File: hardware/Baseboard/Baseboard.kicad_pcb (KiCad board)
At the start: 2 copper layers, 160 x 160 mm, 77 parts, among them IC1 74HC00, IC10 W65C22, IC11 74HC148, IC12 74HC273, IC2 W65C02, IC3 74HC138, IC4 SYSTEM ROM, IC5 RAM, IC6 W65C22, IC7 W65C51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

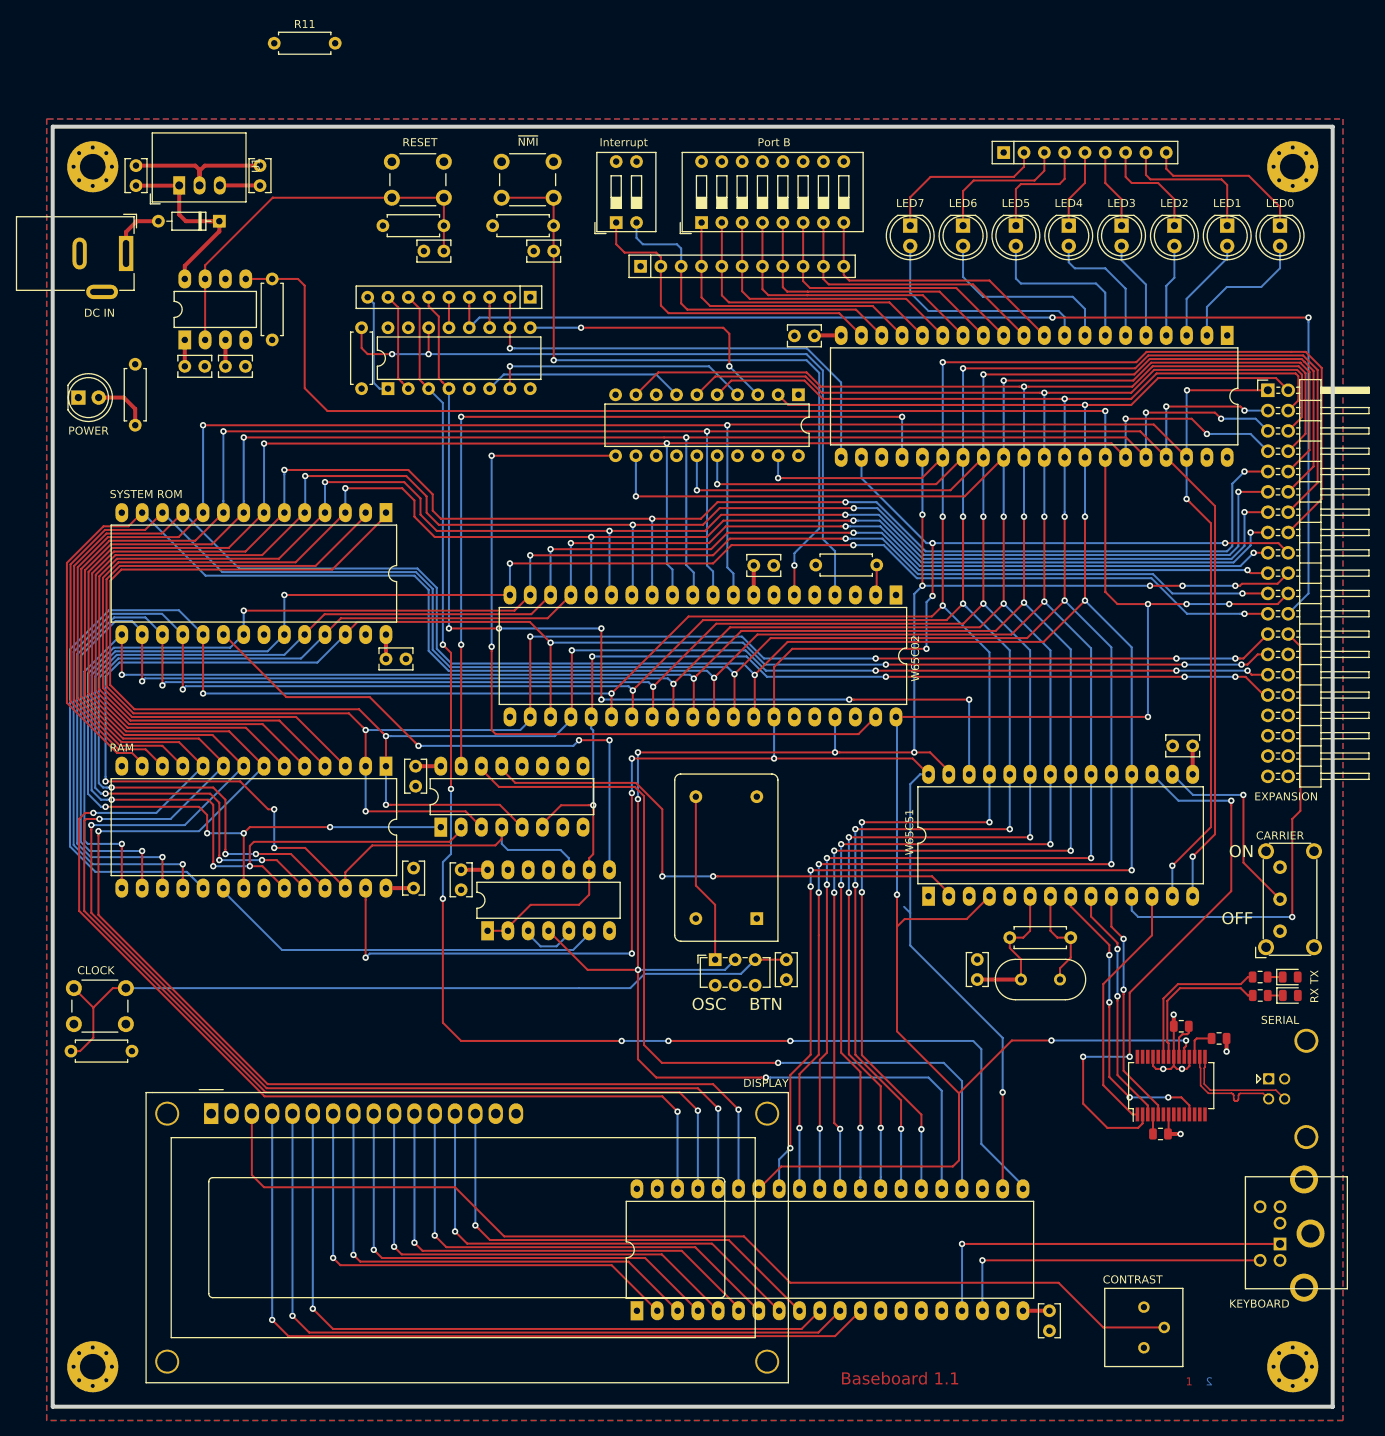
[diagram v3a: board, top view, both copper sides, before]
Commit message: Improve routing, add some datasheet recommendations
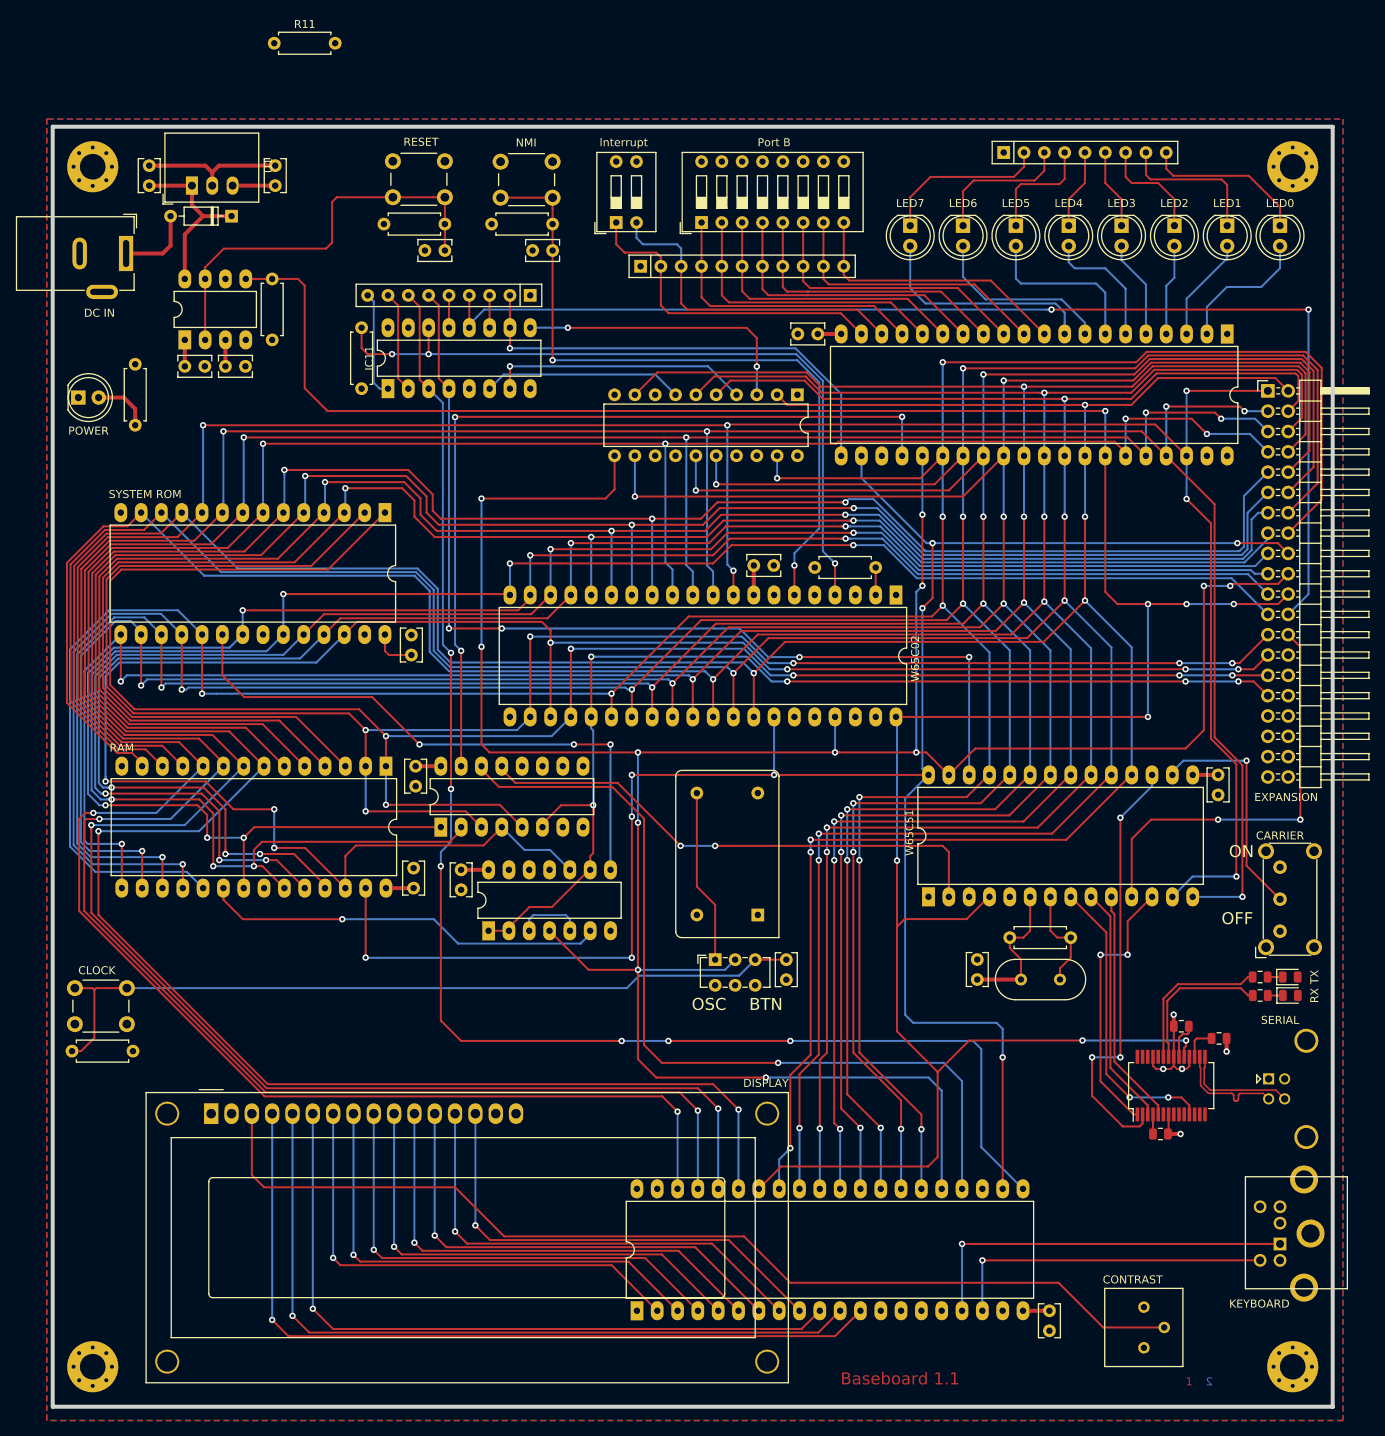
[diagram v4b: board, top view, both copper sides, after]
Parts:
- IC11: footprint Package_DIP:DIP-16_W7.62mm -> Package_DIP:DIP-16_W7.62mm_LongPads
- SW4: value ~NMI -> NMI
- moved C6 4.82 mm to (283.7, 132.3), turned to 270 degrees
- moved C4 3.21 mm to (182.9, 117.3), turned to 90 degrees
- moved C10 1.91 mm to (165.9, 58.7)
- moved C9 1.65 mm to (150.1, 58.7)
- moved D10 1.65 mm to (160.4, 62.5)
- moved U1 1.59 mm to (155.4, 58.7)
- moved C7 0.48 mm to (233.7, 77.2)
- moved XTAL1 0.47 mm to (226.2, 149.8)
- moved R3 0.34 mm to (233.3, 106.4)
- moved R5 0.24 mm to (179.5, 63.5)
- moved R9 0.24 mm to (192.9, 63.5)
- moved RN3 0.23 mm to (197.7, 72.4)
- moved IC6 0.18 mm to (284.9, 77.2)
- moved C17 0.16 mm to (200.5, 66.8)
- moved C11 0.15 mm to (187.1, 66.8)
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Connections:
- net /IO/~NMI renamed /IRQ/~NMI
- IC10 pad 13: Net-(IC10-Pad13) -> (no net)
- IC10 pad 14: Net-(IC10-Pad14) -> (no net)
- IC10 pad 15: Net-(IC10-Pad15) -> (no net)
- IC10 pad 16: Net-(IC10-Pad16) -> (no net)
- IC10 pad 19: Net-(IC10-Pad19) -> (no net)
- IC10 pad 39: Net-(IC10-Pad39) -> (no net)
- IC10 pad 40: Net-(IC10-Pad40) -> (no net)
- IC11 pad 15: Net-(IC11-Pad15) -> (no net)
- IC12 pad 11: /IRQ/IRQ_Sync -> /IO/Clock
- IC12 pad 13: Net-(IC12-Pad13) -> (no net)
- IC12 pad 14: Net-(IC12-Pad14) -> (no net)
- IC12 pad 17: Net-(IC12-Pad17) -> (no net)
- IC12 pad 18: Net-(IC12-Pad18) -> (no net)
- IC12 pad 8: Net-(IC12-Pad8) -> (no net)
- IC2 pad 1: Net-(IC2-Pad1) -> /IRQ/~IRQ_Read
- IC2 pad 3: Net-(IC2-Pad3) -> (no net)
- IC2 pad 35: Net-(IC2-Pad35) -> (no net)
- IC2 pad 36: Net-(IC2-Pad36) -> +5V
- IC2 pad 38: Net-(IC2-Pad38) -> +5V
- IC2 pad 39: /IRQ/IRQ_Sync -> (no net)
- IC2 pad 5: Net-(IC2-Pad5) -> (no net)
- IC2 pad 7: Net-(IC2-Pad7) -> (no net)
- IC3 pad 10: Net-(IC3-Pad10) -> (no net)
- IC3 pad 11: Net-(IC3-Pad11) -> (no net)
- IC3 pad 12: Net-(IC3-Pad12) -> (no net)
- IC3 pad 7: Net-(IC3-Pad7) -> (no net)
- IC3 pad 9: Net-(IC3-Pad9) -> (no net)
- IC6 pad 18: /IO/CB1 -> /IO/CB0
- IC6 pad 19: /IO/CB2 -> /IO/CB1
- IC6 pad 39: Net-(IC6-Pad39) -> (no net)
- IC6 pad 40: Net-(IC6-Pad40) -> (no net)
- IC7 pad 5: Net-(IC7-Pad5) -> (no net)
- IC8 pad 6: Net-(IC8-Pad6) -> (no net)
- IC9 pad 10: Net-(IC9-Pad10) -> (no net)
- IC9 pad 12: Net-(IC9-Pad12) -> (no net)
- IC9 pad 13: Net-(IC9-Pad13) -> (no net)
- IC9 pad 14: Net-(IC9-Pad14) -> (no net)
- IC9 pad 26: Net-(IC9-Pad26) -> (no net)
- IC9 pad 27: Net-(IC9-Pad27) -> (no net)
- IC9 pad 28: Net-(IC9-Pad28) -> (no net)
- IC9 pad 6: Net-(IC9-Pad6) -> (no net)
- IC9 pad 9: Net-(IC9-Pad9) -> (no net)
- RN1 pad 2: /IO/CB2 -> /IO/CB1
- RN1 pad 3: /IO/CB1 -> /IO/CB0
- RV1 pad 3: Net-(RV1-Pad3) -> (no net)
- SW2 pad 1: /IO/CB2 -> /IO/CB1
- SW2 pad 2: /IO/CB1 -> /IO/CB0
- X2 pad 1: Net-(X2-Pad1) -> (no net)
- X3 pad 28: Net-(X3-Pad28) -> (no net)
- X3 pad 30: Net-(X3-Pad30) -> (no net)
- X3 pad 32: Net-(X3-Pad32) -> (no net)
- X3 pad 33: Net-(X3-Pad33) -> (no net)
- X3 pad 34: Net-(X3-Pad34) -> (no net)
- X3 pad 35: Net-(X3-Pad35) -> (no net)
- X3 pad 36: Net-(X3-Pad36) -> (no net)
- X3 pad 37: Net-(X3-Pad37) -> (no net)
- X3 pad 38: Net-(X3-Pad38) -> (no net)
- X4 pad 2: Net-(X4-Pad2) -> (no net)
- X4 pad 6: Net-(X4-Pad6) -> (no net)
- XTAL1 pad 1: Net-(XTAL1-Pad1) -> (no net)
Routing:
- net /IRQ/IRQ_Sync: track 98.9 -> 0.00 mm, vias 2 -> 0
- net /IO/Clock: track 244.6 -> 333.8 mm, vias 11 -> 12
- net /IO/CB2: track 41.6 -> 0.00 mm
- net /IO/CB0: track 0.00 -> 41.6 mm
- net /Processor/~ModemReady: track 70.3 -> 54.5 mm
- net /IO/A1: track 414.8 -> 421.2 mm
- net /IO/A0: track 412.5 -> 418.2 mm, vias 7 -> 8
- net /IO/~TerminalReady: track 58.6 -> 53.0 mm, vias 1 -> 2
- net /IO/R~W: track 269.8 -> 264.3 mm, vias 10 -> 9
- net /IO/D0: track 393.3 -> 388.8 mm, vias 8 -> 7
- net /IO/~CarrierDetect: track 24.9 -> 29.3 mm
- net /IO/D2: track 399.5 -> 395.4 mm, vias 8 -> 7
- net /IO/D1: track 400.4 -> 396.3 mm, vias 8 -> 7
- net Net-(C11-Pad1): track 49.4 -> 52.3 mm
- net /IO/~Reset: track 344.5 -> 341.9 mm
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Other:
- net class Address removed

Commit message: Optimize routing
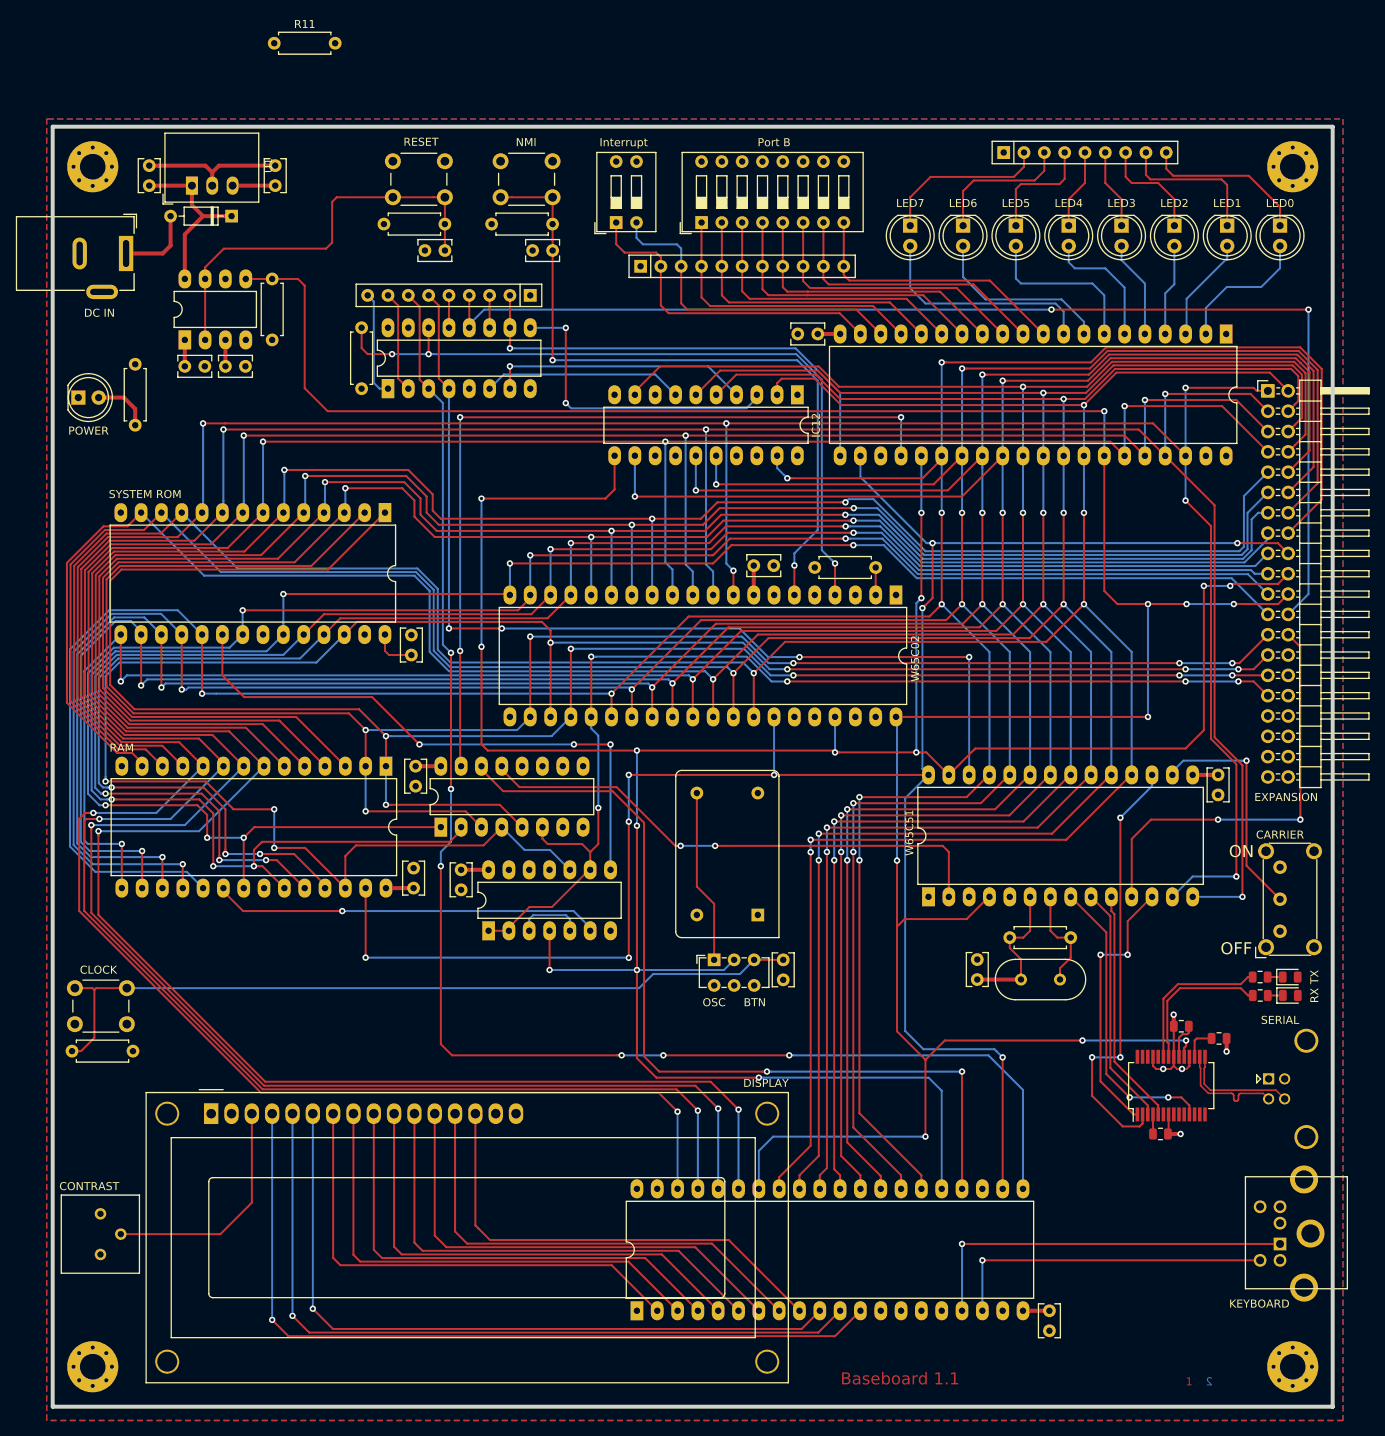
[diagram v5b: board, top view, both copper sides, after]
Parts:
- IC12: footprint Package_DIP:DIP-20_W7.62mm -> Package_DIP:DIP-20_W7.62mm_LongPads
- moved RV1 130.9 mm to (144.0, 192.3)
- moved C19 0.39 mm to (229.4, 155.4)
- moved SW7 0.13 mm to (220.7, 155.4)
- moved IC6 0.13 mm to (284.7, 77.2)
- moved SW4 0.05 mm to (194.0, 55.6)
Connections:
- IC10 pad 13: (no net) -> Net-(IC10-Pad13)
- IC10 pad 14: (no net) -> Net-(IC10-Pad14)
- IC10 pad 15: (no net) -> Net-(IC10-Pad15)
- IC10 pad 16: (no net) -> Net-(IC10-Pad16)
- IC10 pad 19: (no net) -> Net-(IC10-Pad19)
- IC10 pad 39: (no net) -> Net-(IC10-Pad39)
- IC10 pad 40: (no net) -> Net-(IC10-Pad40)
- IC11 pad 15: (no net) -> Net-(IC11-Pad15)
- IC12 pad 13: (no net) -> Net-(IC12-Pad13)
- IC12 pad 14: (no net) -> Net-(IC12-Pad14)
- IC12 pad 17: (no net) -> Net-(IC12-Pad17)
- IC12 pad 18: (no net) -> Net-(IC12-Pad18)
- IC12 pad 8: (no net) -> Net-(IC12-Pad8)
- IC2 pad 3: (no net) -> Net-(IC2-Pad3)
- IC2 pad 35: (no net) -> Net-(IC2-Pad35)
- IC2 pad 39: (no net) -> Net-(IC2-Pad39)
- IC2 pad 5: (no net) -> Net-(IC2-Pad5)
- IC2 pad 7: (no net) -> Net-(IC2-Pad7)
- IC3 pad 10: (no net) -> Net-(IC3-Pad10)
- IC3 pad 11: (no net) -> Net-(IC3-Pad11)
- IC3 pad 12: (no net) -> Net-(IC3-Pad12)
- IC3 pad 7: (no net) -> Net-(IC3-Pad7)
- IC3 pad 9: (no net) -> Net-(IC3-Pad9)
- IC6 pad 39: (no net) -> Net-(IC6-Pad39)
- IC6 pad 40: (no net) -> Net-(IC6-Pad40)
- IC7 pad 5: (no net) -> Net-(IC7-Pad5)
- IC8 pad 6: (no net) -> Net-(IC8-Pad6)
- IC9 pad 10: (no net) -> Net-(IC9-Pad10)
- IC9 pad 12: (no net) -> Net-(IC9-Pad12)
- IC9 pad 13: (no net) -> Net-(IC9-Pad13)
- IC9 pad 14: (no net) -> Net-(IC9-Pad14)
- IC9 pad 26: (no net) -> Net-(IC9-Pad26)
- IC9 pad 27: (no net) -> Net-(IC9-Pad27)
- IC9 pad 28: (no net) -> Net-(IC9-Pad28)
- IC9 pad 6: (no net) -> Net-(IC9-Pad6)
- IC9 pad 9: (no net) -> Net-(IC9-Pad9)
- RV1 pad 3: (no net) -> Net-(RV1-Pad3)
- X2 pad 1: (no net) -> Net-(X2-Pad1)
- X3 pad 28: (no net) -> Net-(X3-Pad28)
- X3 pad 30: (no net) -> Net-(X3-Pad30)
- X3 pad 32: (no net) -> Net-(X3-Pad32)
- X3 pad 33: (no net) -> Net-(X3-Pad33)
- X3 pad 34: (no net) -> Net-(X3-Pad34)
- X3 pad 35: (no net) -> Net-(X3-Pad35)
- X3 pad 36: (no net) -> Net-(X3-Pad36)
- X3 pad 37: (no net) -> Net-(X3-Pad37)
- X3 pad 38: (no net) -> Net-(X3-Pad38)
- X4 pad 2: (no net) -> Net-(X4-Pad2)
- X4 pad 6: (no net) -> Net-(X4-Pad6)
- XTAL1 pad 1: (no net) -> Net-(XTAL1-Pad1)
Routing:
- net Net-(DS1-Pad3): track 129.6 -> 29.5 mm
- net Net-(IC11-Pad9): track 35.9 -> 38.9 mm
- net /IO/Clock: track 333.8 -> 336.8 mm, vias 12 -> 13
- net /IO/A1: track 421.2 -> 424.1 mm, vias 7 -> 6
- net /IO/D0: track 388.8 -> 391.6 mm, vias 7 -> 6
- net /IO/A2: track 358.6 -> 361.2 mm, vias 6 -> 5
- net /IO/A3: track 362.1 -> 364.5 mm, vias 6 -> 5
- net Net-(IC1-Pad6): track 50.5 -> 48.5 mm
- net /IRQ/~IRQ_VIA_2: track 182.1 -> 183.8 mm
- net /IO/A15: track 137.2 -> 138.5 mm
- net /Processor/~CS_VIA_2: track 106.7 -> 107.9 mm, vias 1 -> 2
- net /IO/A0: track 418.2 -> 419.3 mm
- net /Processor/~CS_VIA_1: track 104.7 -> 103.6 mm
- net /IO/D3: track 393.1 -> 394.1 mm, vias 9 -> 8
- net /IO/D2: track 395.4 -> 396.1 mm, vias 7 -> 6
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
